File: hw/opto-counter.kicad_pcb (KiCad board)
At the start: 2 copper layers, 27.9 x 27.9 mm, 13 parts, among them J1 IR-REC, J2 qwiic, J3 UPDI, U1 ATtiny3224-SS, U2 TSSP6038

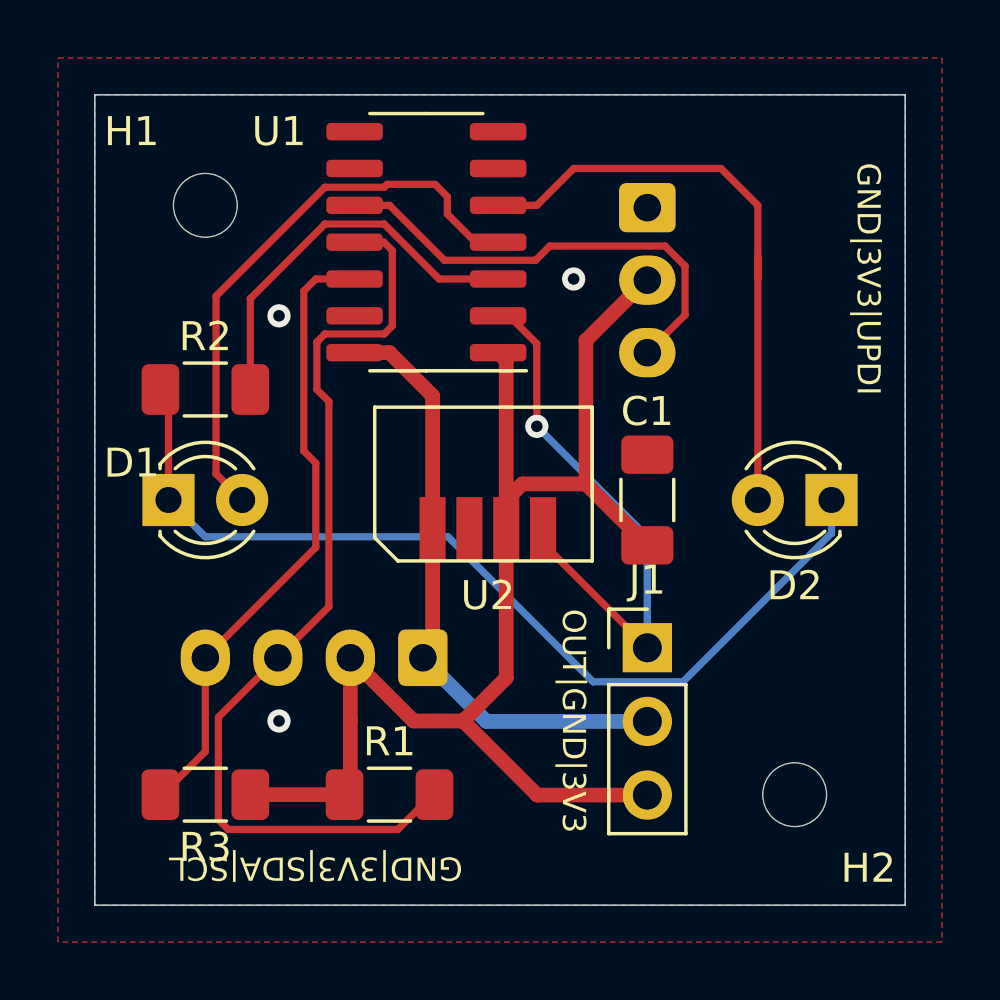
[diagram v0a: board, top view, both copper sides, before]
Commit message: Fix the schematic to connect the led to the PB0 (WO0) PWM output of TCA
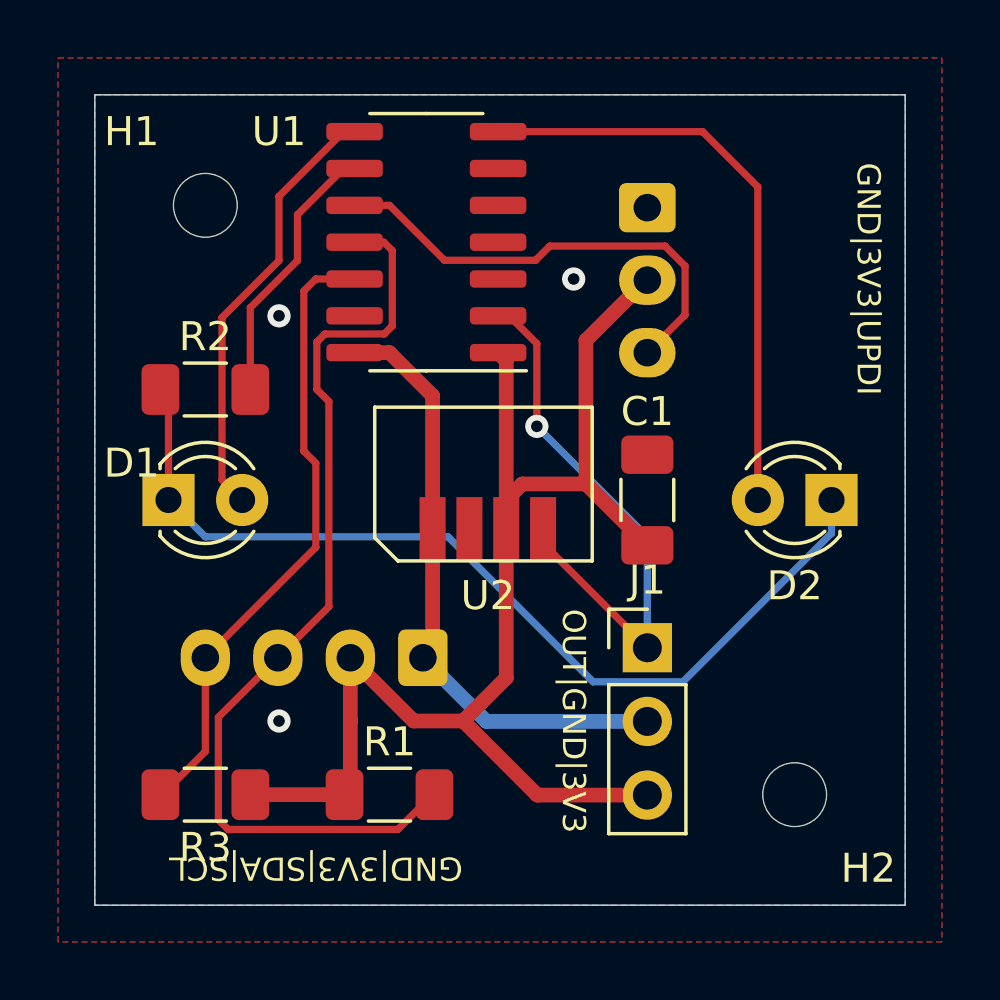
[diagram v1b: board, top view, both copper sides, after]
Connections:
- R2 pad 2: Net-(U1-PA5) -> Net-(U1-PB0)
- U1 pad 3: Net-(U1-PA5) -> unconnected-(U1-PA5-Pad3)
- U1 pad 4: Net-(D1-A) -> unconnected-(U1-PA6-Pad4)
- U1 pad 5: Net-(D2-A) -> unconnected-(U1-PA7-Pad5)
- U1 pad 7: unconnected-(U1-PB2-Pad7) -> Net-(D2-A)
- U1 pad 8: unconnected-(U1-PB1-Pad8) -> Net-(D1-A)
- U1 pad 9: unconnected-(U1-PB0-Pad9) -> Net-(U1-PB0)
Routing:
- net Net-(U1-PA5): track 13.5 -> 0.00 mm
- net Net-(U1-PB0): track 0.00 -> 9.33 mm
- net Net-(D1-A): track 19.9 -> 15.1 mm
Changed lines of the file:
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@@
   (net 7 "SCL")
   (net 8 "UPDI")
-  (net 9 "Net-(U1-PA5)")
+  (net 9 "Net-(U1-PB0)")
   (net 10 "Net-(J1-Pin_1)")
   (net 11 "unconnected-(U1-PB3-Pad6)")
-  (net 12 "unconnected-(U1-PB2-Pad7)")
-  (net 13 "unconnected-(U1-PB1-Pad8)")
-  (net 14 "unconnected-(U1-PB0-Pad9)")
+  (net 12 "unconnected-(U1-PA5-Pad3)")
+  (net 13 "unconnected-(U1-PA6-Pad4)")
+  (net 14 "unconnected-(U1-PA7-Pad5)")
   (net 15 "unconnected-(U1-PA3-Pad13)")
   (net 16 "unconnected-(U2-Pad2)")
@@
       (net 3 "Net-(D1-K)") (pintype "passive"))
     (pad "2" smd roundrect (at 1.55 0) (size 1.3 1.75) (layers "F.Cu" "F.Paste" "F.Mask") (roundrect_rratio 0.1923076923)
-      (net 9 "Net-(U1-PA5)") (pintype "passive"))
+      (net 9 "Net-(U1-PB0)") (pintype "passive"))
     (model "${KICAD6_3DMODEL_DIR}/Resistor_SMD.3dshapes/R_1206_3216Metric.wrl"
       (offset (xyz 0 0 0))
@@
       (net 10 "Net-(J1-Pin_1)") (pinfunction "PA4") (pintype "bidirectional"))
     (pad "3" smd roundrect (at -2.475 -1.27 180) (size 1.95 0.6) (layers "F.Cu" "F.Paste" "F.Mask") (roundrect_rratio 0.25)
-      (net 9 "Net-(U1-PA5)") (pinfunction "PA5") (pintype "bidirectional"))
+      (net 12 "unconnected-(U1-PA5-Pad3)") (pinfunction "PA5") (pintype "bidirectional+no_connect"))
     (pad "4" smd roundrect (at -2.475 0 180) (size 1.95 0.6) (layers "F.Cu" "F.Paste" "F.Mask") (roundrect_rratio 0.25)
-      (net 4 "Net-(D1-A)") (pinfunction "PA6") (pintype "bidirectional"))
+      (net 13 "unconnected-(U1-PA6-Pad4)") (pinfunction "PA6") (pintype "bidirectional+no_connect"))
     (pad "5" smd roundrect (at -2.475 1.27 180) (size 1.95 0.6) (layers "F.Cu" "F.Paste" "F.Mask") (roundrect_rratio 0.25)
-      (net 5 "Net-(D2-A)") (pinfunction "PA7") (pintype "bidirectional"))
+      (net 14 "unconnected-(U1-PA7-Pad5)") (pinfunction "PA7") (pintype "bidirectional+no_connect"))
     (pad "6" smd roundrect (at -2.475 2.54 180) (size 1.95 0.6) (layers "F.Cu" "F.Paste" "F.Mask") (roundrect_rratio 0.25)
       (net 11 "unconnected-(U1-PB3-Pad6)") (pinfunction "PB3") (pintype "bidirectional+no_connect"))
     (pad "7" smd roundrect (at -2.475 3.81 180) (size 1.95 0.6) (layers "F.Cu" "F.Paste" "F.Mask") (roundrect_rratio 0.25)
-      (net 12 "unconnected-(U1-PB2-Pad7)") (pinfunction "PB2") (pintype "bidirectional+no_connect"))
+      (net 5 "Net-(D2-A)") (pinfunction "PB2") (pintype "bidirectional"))
     (pad "8" smd roundrect (at 2.475 3.81 180) (size 1.95 0.6) (layers "F.Cu" "F.Paste" "F.Mask") (roundrect_rratio 0.25)
-      (net 13 "unconnected-(U1-PB1-Pad8)") (pinfunction "PB1") (pintype "bidirectional+no_connect"))
+      (net 4 "Net-(D1-A)") (pinfunction "PB1") (pintype "bidirectional"))
     (pad "9" smd roundrect (at 2.475 2.54 180) (size 1.95 0.6) (layers "F.Cu" "F.Paste" "F.Mask") (roundrect_rratio 0.25)
-      (net 14 "unconnected-(U1-PB0-Pad9)") (pinfunction "PB0") (pintype "bidirectional+no_connect"))
+      (net 9 "Net-(U1-PB0)") (pinfunction "PB0") (pintype "bidirectional"))
     (pad "10" smd roundrect (at 2.475 1.27 180) (size 1.95 0.6) (layers "F.Cu" "F.Paste" "F.Mask") (roundrect_rratio 0.25)
       (net 8 "UPDI") (pinfunction "~{RESET}/PA0") (pintype "bidirectional"))
@@
   (segment (start 83.78 44.37) (end 80.681299 44.37) (width 0.25) (layer "B.Cu") (net 3))
   (segment (start 88.9 38.1) (end 88.9 39.25) (width 0.25) (layer "B.Cu") (net 3))
-  (segment (start 75.655 27.639695) (end 75.230305 27.215) (width 0.25) (layer "F.Cu") (net 4))
-  (segment (start 75.655 28.240305) (end 75.655 27.639695) (width 0.25) (layer "F.Cu") (net 4))
-  (segment (start 67.68 37.2) (end 67.68 31.068249) (width 0.25) (layer "F.Cu") (net 4))
-  (segment (start 73.576751 27.215) (end 73.476751 27.315) (width 0.25) (layer "F.Cu") (net 4))
-  (segment (start 73.476751 27.315) (end 71.433249 27.315) (width 0.25) (layer "F.Cu") (net 4))
-  (segment (start 77.405 29.21) (end 76.624695 29.21) (width 0.25) (layer "F.Cu") (net 4))
-  (segment (start 76.624695 29.21) (end 75.655 28.240305) (width 0.25) (layer "F.Cu") (net 4))
-  (segment (start 75.230305 27.215) (end 73.576751 27.215) (width 0.25) (layer "F.Cu") (net 4))
-  (segment (start 68.58 38.1) (end 67.68 37.2) (width 0.25) (layer "F.Cu") (net 4))
-  (segment (start 67.68 31.068249) (end 71.433249 27.315) (width 0.25) (layer "F.Cu") (net 4))
-  (segment (start 83.338173 26.67) (end 83.82 26.67) (width 0.25) (layer "F.Cu") (net 5))
-  (segment (start 86.36 38.1) (end 86.36 29.691827) (width 0.25) (layer "F.Cu") (net 5))
-  (segment (start 78.74 27.94) (end 77.405 27.94) (width 0.25) (layer "F.Cu") (net 5))
-  (segment (start 83.82 26.67) (end 85.09 26.67) (width 0.25) (layer "F.Cu") (net 5))
-  (segment (start 83.338173 26.67) (end 80.01 26.67) (width 0.25) (layer "F.Cu") (net 5))
-  (segment (start 80.01 26.67) (end 78.74 27.94) (width 0.25) (layer "F.Cu") (net 5))
-  (segment (start 86.36 27.94) (end 86.36 30.48) (width 0.25) (layer "F.Cu") (net 5))
-  (segment (start 85.09 26.67) (end 86.36 27.94) (width 0.25) (layer "F.Cu") (net 5))
+  (segment (start 72.078249 25.4) (end 69.849302 27.628947) (width 0.25) (layer "F.Cu") (net 4))
+  (segment (start 67.885 31.808604) (end 67.885 37.405) (width 0.25) (layer "F.Cu") (net 4))
+  (segment (start 69.849302 29.844302) (end 67.885 31.808604) (width 0.25) (layer "F.Cu") (net 4))
+  (segment (start 72.455 25.4) (end 72.078249 25.4) (width 0.25) (layer "F.Cu") (net 4))
+  (segment (start 69.849302 27.628947) (end 69.849302 29.844302) (width 0.25) (layer "F.Cu") (net 4))
+  (segment (start 67.885 37.405) (end 68.58 38.1) (width 0.25) (layer "F.Cu") (net 4))
+  (segment (start 86.36 38.1) (end 86.36 27.305) (width 0.25) (layer "F.Cu") (net 5))
+  (segment (start 86.36 27.305) (end 84.455 25.4) (width 0.25) (layer "F.Cu") (net 5))
+  (segment (start 86.36 38.1) (end 86.995 38.1) (width 0.25) (layer "F.Cu") (net 5))
+  (segment (start 84.455 25.4) (end 77.405 25.4) (width 0.25) (layer "F.Cu") (net 5))
   (segment (start 73.755 29.499645) (end 73.755 32.096751) (width 0.25) (layer "F.Cu") (net 6))
   (segment (start 67.76 45.59) (end 67.76 49.123172) (width 0.25) (layer "F.Cu") (net 6))
@@
   (segment (start 83.85 31.72) (end 83.85 30.033299) (width 0.25) (layer "F.Cu") (net 8))
   (segment (start 82.55 33.02) (end 83.85 31.72) (width 0.25) (layer "F.Cu") (net 8))
-  (segment (start 73.476751 28.585) (end 71.433249 28.585) (width 0.25) (layer "F.Cu") (net 9))
-  (segment (start 68.86 34.29) (end 68.86 31.158249) (width 0.25) (layer "F.Cu") (net 9))
-  (segment (start 77.405 30.48) (end 75.371751 30.48) (width 0.25) (layer "F.Cu") (net 9))
-  (segment (start 68.86 31.158249) (end 71.433249 28.585) (width 0.25) (layer "F.Cu") (net 9))
-  (segment (start 75.371751 30.48) (end 73.476751 28.585) (width 0.25) (layer "F.Cu") (net 9))
+  (segment (start 72.078249 26.67) (end 72.455 26.67) (width 0.25) (layer "F.Cu") (net 9))
+  (segment (start 68.86 34.29) (end 68.86 31.47) (width 0.25) (layer "F.Cu") (net 9))
+  (segment (start 68.86 31.47) (end 70.485 29.845) (width 0.25) (layer "F.Cu") (net 9))
+  (segment (start 70.485 28.263249) (end 72.078249 26.67) (width 0.25) (layer "F.Cu") (net 9))
+  (segment (start 70.485 29.845) (end 70.485 28.263249) (width 0.25) (layer "F.Cu") (net 9))
   (segment (start 78.74 32.708249) (end 77.781751 31.75) (width 0.25) (layer "F.Cu") (net 10))
   (segment (start 78.74 35.56) (end 78.74 32.708249) (width 0.25) (layer "F.Cu") (net 10))

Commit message: Update the PCB with the new pin assignments
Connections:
- D2 pad 1: Net-(D1-K) -> Net-(D2-K)
- D2 pad 2: Net-(D2-A) -> Net-(D1-A)
- J1 pad 1: Net-(J1-Pin_1) -> OPT
- R1 pad 2: SDA -> SCL
- R2 pad 1: Net-(D1-K) -> Net-(D1-A)
- R2 pad 2: Net-(U1-PB0) -> Net-(U1-PB3)
- R3 pad 2: SCL -> SDA
- U1 pad 11: SDA -> unconnected-(U1-PA1-Pad11)
- U1 pad 12: SCL -> unconnected-(U1-PA2-Pad12)
- U1 pad 2: Net-(J1-Pin_1) -> unconnected-(U1-PA4-Pad2)
- U1 pad 3: unconnected-(U1-PA5-Pad3) -> Net-(D1-K)
- U1 pad 4: unconnected-(U1-PA6-Pad4) -> Net-(D2-K)
- U1 pad 6: unconnected-(U1-PB3-Pad6) -> Net-(U1-PB3)
- U1 pad 7: Net-(D2-A) -> OPT
- U1 pad 8: Net-(D1-A) -> SDA
- U1 pad 9: Net-(U1-PB0) -> SCL
- U2 pad 4: Net-(J1-Pin_1) -> OPT
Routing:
- net OPT: track 0.00 -> 39.6 mm
- net Net-(D2-K): track 0.00 -> 23.9 mm
- net Net-(D2-A): track 21.2 -> 0.00 mm
- net Net-(J1-Pin_1): track 19.4 -> 0.00 mm, vias 1 -> 0
- net Net-(D1-K): track 32.7 -> 14.5 mm, vias 0 -> 1
- net Net-(U1-PB3): track 0.00 -> 17.3 mm
- net SCL: track 21.7 -> 37.3 mm
- net Net-(U1-PB0): track 9.33 -> 0.00 mm
- net Net-(D1-A): track 15.1 -> 23.4 mm
- net SDA: track 33.1 -> 28.7 mm

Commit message: Small improvements of the PCB before producing prototype v2
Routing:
- net SDA: track 28.7 -> 26.6 mm
- net Net-(D1-A): track 23.4 -> 22.8 mm
- net GND: vias 3 -> 2
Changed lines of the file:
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@@
         (effects (font (size 1 1) (thickness 0.15)))
     )
-    (fp_text value "MountingHole" (at 0 3.2) (layer "F.Fab")
+    (fp_text value "MountingHole" (at 0 3.2) (layer "F.Fab") hide
         (effects (font (size 1 1) (thickness 0.15)))
     )
@@
   (segment (start 75.145 42.965) (end 75.145 39.1) (width 0.508) (layer "F.Cu") (net 2))
   (segment (start 73.66 33.02) (end 72.455 33.02) (width 0.508) (layer "F.Cu") (net 2))
-  (via (at 69.85 45.72) (size 0.8) (drill 0.4) (layers "F.Cu" "B.Cu") (free) (net 2))
   (via (at 80.01 30.48) (size 0.8) (drill 0.4) (layers "F.Cu" "B.Cu") (free) (net 2))
-  (via (at 69.85 31.75) (size 0.8) (drill 0.4) (layers "F.Cu" "B.Cu") (free) (net 2))
+  (via (at 71.12 46.355) (size 0.8) (drill 0.4) (layers "F.Cu" "B.Cu") (net 2))
   (segment (start 77.005 45.735) (end 74.81 43.54) (width 0.508) (layer "B.Cu") (net 2))
   (segment (start 82.55 45.735) (end 77.005 45.735) (width 0.508) (layer "B.Cu") (net 2))
@@
   (segment (start 69.85 36.195) (end 67.945 36.195) (width 0.25) (layer "B.Cu") (net 3))
   (segment (start 74.93 31.115) (end 69.85 36.195) (width 0.25) (layer "B.Cu") (net 3))
-  (segment (start 86.36 38.1) (end 86.995 38.1) (width 0.25) (layer "F.Cu") (net 4))
   (segment (start 65.76 35.28) (end 65.76 34.29) (width 0.25) (layer "F.Cu") (net 4))
   (segment (start 68.58 38.1) (end 65.76 35.28) (width 0.25) (layer "F.Cu") (net 4))
@@
   (segment (start 88.9 28.575) (end 88.9 38.1) (width 0.25) (layer "F.Cu") (net 5))
   (segment (start 81.591751 25.4) (end 85.725 25.4) (width 0.25) (layer "F.Cu") (net 5))
-  (segment (start 73.66 25.4) (end 72.455 25.4) (width 0.25) (layer "F.Cu") (net 6))
-  (segment (start 71.155 27.593249) (end 71.453249 27.295) (width 0.25) (layer "F.Cu") (net 6))
-  (segment (start 73.755 25.495) (end 73.66 25.4) (width 0.25) (layer "F.Cu") (net 6))
-  (segment (start 73.67 27.295) (end 73.755 27.21) (width 0.25) (layer "F.Cu") (net 6))
-  (segment (start 69.81 43.54) (end 71.155 42.195) (width 0.25) (layer "F.Cu") (net 6))
-  (segment (start 71.155 42.195) (end 71.155 27.593249) (width 0.25) (layer "F.Cu") (net 6))
-  (segment (start 73.755 27.21) (end 73.755 25.495) (width 0.25) (layer "F.Cu") (net 6))
-  (segment (start 71.453249 27.295) (end 73.67 27.295) (width 0.25) (layer "F.Cu") (net 6))
-  (segment (start 65.76 48.26) (end 65.76 47.59) (width 0.25) (layer "F.Cu") (net 6))
-  (segment (start 65.76 47.59) (end 69.81 43.54) (width 0.25) (layer "F.Cu") (net 6))
-  (segment (start 73.94 49.53) (end 75.21 48.26) (width 0.25) (layer "F.Cu") (net 7))
-  (segment (start 64.785 49.123173) (end 65.191827 49.53) (width 0.25) (layer "F.Cu") (net 7))
-  (segment (start 64.785 46.065) (end 64.785 49.123173) (width 0.25) (layer "F.Cu") (net 7))
-  (segment (start 65.191827 49.53) (end 73.94 49.53) (width 0.25) (layer "F.Cu") (net 7))
+  (segment (start 66.675 45.085) (end 68.265 45.085) (width 0.25) (layer "F.Cu") (net 6))
+  (segment (start 66.04 42.372412) (end 69.85 38.562412) (width 0.25) (layer "F.Cu") (net 6))
+  (segment (start 72.075457 25.4) (end 72.455 25.4) (width 0.25) (layer "F.Cu") (net 6))
+  (segment (start 69.85 38.562412) (end 69.85 27.625457) (width 0.25) (layer "F.Cu") (net 6))
+  (segment (start 69.85 27.625457) (end 72.075457 25.4) (width 0.25) (layer "F.Cu") (net 6))
+  (segment (start 66.04 44.45) (end 66.675 45.085) (width 0.25) (layer "F.Cu") (net 6))
+  (segment (start 66.04 42.372412) (end 66.04 44.45) (width 0.25) (layer "F.Cu") (net 6))
+  (segment (start 68.265 45.085) (end 69.81 43.54) (width 0.25) (layer "F.Cu") (net 6))
+  (segment (start 70.03 40.82) (end 69.7125 41.1375) (width 0.25) (layer "F.Cu") (net 7))
+  (segment (start 74.01 49.46) (end 68.221827 49.46) (width 0.25) (layer "F.Cu") (net 7))
+  (segment (start 67.885 47.251701) (end 70.985 44.151701) (width 0.25) (layer "F.Cu") (net 7))
   (segment (start 72.455 26.67) (end 71.441853 26.67) (width 0.25) (layer "F.Cu") (net 7))
+  (segment (start 70.985 44.151701) (end 70.985 42.41) (width 0.25) (layer "F.Cu") (net 7))
+  (segment (start 70.705 40.145) (end 70.03 40.82) (width 0.25) (layer "F.Cu") (net 7))
   (segment (start 71.441853 26.67) (end 70.705 27.406853) (width 0.25) (layer "F.Cu") (net 7))
-  (segment (start 70.705 40.145) (end 67.31 43.54) (width 0.25) (layer "F.Cu") (net 7))
-  (segment (start 67.31 43.54) (end 64.785 46.065) (width 0.25) (layer "F.Cu") (net 7))
+  (segment (start 67.885 49.123173) (end 67.885 47.251701) (width 0.25) (layer "F.Cu") (net 7))
+  (segment (start 69.7125 41.1375) (end 68.4425 42.4075) (width 0.25) (layer "F.Cu") (net 7))
+  (segment (start 68.221827 49.46) (end 67.885 49.123173) (width 0.25) (layer "F.Cu") (net 7))
+  (segment (start 75.21 48.26) (end 74.01 49.46) (width 0.25) (layer "F.Cu") (net 7))
+  (segment (start 70.985 42.41) (end 69.7125 41.1375) (width 0.25) (layer "F.Cu") (net 7))
+  (segment (start 68.4425 42.4075) (end 67.31 43.54) (width 0.25) (layer "F.Cu") (net 7))
   (segment (start 70.705 27.406853) (end 70.705 40.145) (width 0.25) (layer "F.Cu") (net 7))
   (segment (start 83.85 30.033299) (end 83.161701 29.345) (width 0.25) (layer "F.Cu") (net 8))
@@
   (segment (start 78.955 39.1) (end 78.955 39.6) (width 0.25) (layer "F.Cu") (net 9))
   (segment (start 85.911396 24.95) (end 90.125 29.163604) (width 0.25) (layer "F.Cu") (net 9))
-  (segment (start 76.835 26.67) (end 77.405 26.67) (width 0.25) (layer "F.Cu") (net 10))
-  (segment (start 68.86 27.348249) (end 71.443249 24.765) (width 0.25) (layer "F.Cu") (net 10))
-  (segment (start 71.443249 24.765) (end 74.93 24.765) (width 0.25) (layer "F.Cu") (net 10))
-  (segment (start 74.93 24.765) (end 76.835 26.67) (width 0.25) (layer "F.Cu") (net 10))
-  (segment (start 68.86 34.29) (end 68.86 27.348249) (width 0.25) (layer "F.Cu") (net 10))
+  (segment (start 77.405 26.67) (end 76.835 26.67) (width 0.25) (layer "F.Cu") (net 10))
+  (segment (start 71.443249 24.765) (end 69.4 26.808249) (width 0.25) (layer "F.Cu") (net 10))
+  (segment (start 76.835 26.67) (end 74.93 24.765) (width 0.25) (layer "F.Cu") (net 10))
+  (segment (start 69.4 33.75) (end 68.86 34.29) (width 0.25) (layer "F.Cu") (net 10))
+  (segment (start 69.4 26.808249) (end 69.4 33.75) (width 0.25) (layer "F.Cu") (net 10))
+  (segment (start 74.93 24.765) (end 71.443249 24.765) (width 0.25) (layer "F.Cu") (net 10))
   (zone (net 2) (net_name "GND") (layer "F.Cu") (hatch edge 0.508)
     (connect_pads (clearance 0.508))
     (min_thickness 0.254) (filled_areas_thickness no)
-    (fill (thermal_gap 0.508) (thermal_bridge_width 0.508))
+    (fill yes (thermal_gap 0.508) (thermal_bridge_width 0.508))
     (polygon
       (pts
@@
     (connect_pads (clearance 0.508))
     (min_thickness 0.254) (filled_areas_thickness no)
-    (fill (thermal_gap 0.508) (thermal_bridge_width 0.508))
+    (fill yes (thermal_gap 0.508) (thermal_bridge_width 0.508))
     (polygon
       (pts

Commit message: Some more work on fixing the PCB
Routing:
- net SDA: track 26.6 -> 31.0 mm
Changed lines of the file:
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@@
   (segment (start 88.9 28.575) (end 88.9 38.1) (width 0.25) (layer "F.Cu") (net 5))
   (segment (start 81.591751 25.4) (end 85.725 25.4) (width 0.25) (layer "F.Cu") (net 5))
-  (segment (start 66.675 45.085) (end 68.265 45.085) (width 0.25) (layer "F.Cu") (net 6))
-  (segment (start 66.04 42.372412) (end 69.85 38.562412) (width 0.25) (layer "F.Cu") (net 6))
-  (segment (start 72.075457 25.4) (end 72.455 25.4) (width 0.25) (layer "F.Cu") (net 6))
-  (segment (start 69.85 38.562412) (end 69.85 27.625457) (width 0.25) (layer "F.Cu") (net 6))
-  (segment (start 69.85 27.625457) (end 72.075457 25.4) (width 0.25) (layer "F.Cu") (net 6))
-  (segment (start 66.04 44.45) (end 66.675 45.085) (width 0.25) (layer "F.Cu") (net 6))
-  (segment (start 66.04 42.372412) (end 66.04 44.45) (width 0.25) (layer "F.Cu") (net 6))
-  (segment (start 68.265 45.085) (end 69.81 43.54) (width 0.25) (layer "F.Cu") (net 6))
+  (segment (start 66.04 47.98) (end 66.04 45.085) (width 0.25) (layer "F.Cu") (net 6))
+  (segment (start 68.265 45.085) (end 66.04 45.085) (width 0.25) (layer "F.Cu") (net 6))
+  (segment (start 72.075457 25.4) (end 69.85 27.625457) (width 0.25) (layer "F.Cu") (net 6))
+  (segment (start 67.945 41.91) (end 66.675 41.91) (width 0.25) (layer "F.Cu") (net 6))
+  (segment (start 65.76 48.26) (end 66.04 47.98) (width 0.25) (layer "F.Cu") (net 6))
+  (segment (start 69.81 43.54) (end 68.265 45.085) (width 0.25) (layer "F.Cu") (net 6))
+  (segment (start 66.675 41.91) (end 66.04 42.545) (width 0.25) (layer "F.Cu") (net 6))
+  (segment (start 69.85 40.005) (end 67.945 41.91) (width 0.25) (layer "F.Cu") (net 6))
+  (segment (start 69.85 27.625457) (end 69.85 40.005) (width 0.25) (layer "F.Cu") (net 6))
+  (segment (start 66.04 42.545) (end 66.04 45.085) (width 0.25) (layer "F.Cu") (net 6))
+  (segment (start 72.455 25.4) (end 72.075457 25.4) (width 0.25) (layer "F.Cu") (net 6))
   (segment (start 70.03 40.82) (end 69.7125 41.1375) (width 0.25) (layer "F.Cu") (net 7))
   (segment (start 74.01 49.46) (end 68.221827 49.46) (width 0.25) (layer "F.Cu") (net 7))
